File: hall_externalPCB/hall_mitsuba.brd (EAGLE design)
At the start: 100 x 100 mm, 7 parts, among them J1 HEADER_SIDE_5POS, U1 HALLSOT23W, U2 HALLSOT23W, U3 HALLSOT23W

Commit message: placed 8-pin connector
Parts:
- added U$1: HEADER8DEFAULT, Custom_new:8PINVALULOK
- moved J1 35.2 mm to (9.94, 30.5)
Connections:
- removed net N$2: J1.1, U1.2
- removed net N$4: J1.3, U3.2
- removed net N$7: J1.2, U2.2
- new net HALL_A: J1.1, U$1.4, U1.2
- new net HALL_B: J1.2, U$1.3, U2.2
- new net HALL_C: J1.3, U$1.5, U3.2
- net +5V: now also U$1.2
- net GND: now also U$1.1
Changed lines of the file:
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@@
 <drawing>
 <settings>
-<setting alwaysvectorfont="yes"/>
+<setting alwaysvectorfont="no"/>
 <setting verticaltext="up"/>
 </settings>
@@
 <element name="C2" library="rcl" package="C0603" value="0.1uF" x="-31.568" y="31.57" rot="MR315"/>
 <element name="C3" library="rcl" package="C0603" value="0.1uF" x="-27.217996875" y="35.57" rot="MR322.5"/>
-<element name="J1" library="sc_usercreated" package="HEADER_SIDE_5POS" value="HEADER_SIDE_5POS" x="-24.06" y="21.48"/>
+<element name="J1" library="sc_usercreated" package="HEADER_SIDE_5POS" value="HEADER_SIDE_5POS" x="9.94" y="30.48"/>
 <element name="U1" library="Custom_new" package="SOT23W" value="HALLSOT23W" x="-38.080959375" y="29.22055" rot="MR307.5"/>
 <element name="U2" library="Custom_new" package="SOT23W" value="HALLSOT23W" x="-33.941125" y="33.941125" rot="MR315"/>
 <element name="U3" library="Custom_new" package="SOT23W" value="HALLSOT23W" x="-29.22055" y="38.080959375" rot="MR322.5"/>
+<element name="U$1" library="Custom_new" package="8PINVALULOK" value="HEADER8DEFAULT" x="-20.099509375" y="11.189965625" rot="R45"/>
 </elements>
 <signals>
@@
 <contactref element="C3" pad="1"/>
 <contactref element="J1" pad="4"/>
-<wire x1="-27.67365" y1="37.62554375" x2="-24.06" y2="18.94" width="0" layer="19" extent="1-1"/>
-<wire x1="-32.348015625" y1="33.691515625" x2="-27.67365" y2="37.62554375" width="0" layer="19" extent="1-1"/>
-<wire x1="-36.468896875" y1="29.18101875" x2="-32.348015625" y2="33.691515625" width="0" layer="19" extent="1-1"/>
-<wire x1="-34.90055" y1="27.85435" x2="-27.67365" y2="37.62554375" width="0" layer="19" extent="1-1"/>
-<wire x1="-30.966959375" y1="32.171040625" x2="-36.468896875" y2="29.18101875" width="0" layer="19" extent="1-1"/>
-<wire x1="-26.543646875" y1="36.087446875" x2="-30.966959375" y2="32.171040625" width="0" layer="19" extent="1-1"/>
+<contactref element="U$1" pad="2"/>
+<wire x1="-20.099509375" y1="11.189965625" x2="9.94" y2="27.94" width="0" layer="19" extent="1-1"/>
+<wire x1="-34.90055" y1="27.85435" x2="-20.099509375" y2="11.189965625" width="0" layer="19" extent="16-16"/>
+<wire x1="-36.468896875" y1="29.18101875" x2="-34.90055" y2="27.85435" width="0" layer="19" extent="16-16"/>
+<wire x1="-30.966959375" y1="32.171040625" x2="-34.90055" y2="27.85435" width="0" layer="19" extent="16-16"/>
+<wire x1="-32.348015625" y1="33.691515625" x2="-30.966959375" y2="32.171040625" width="0" layer="19" extent="16-16"/>
+<wire x1="-26.543646875" y1="36.087446875" x2="-30.966959375" y2="32.171040625" width="0" layer="19" extent="16-16"/>
+<wire x1="-27.67365" y1="37.625540625" x2="-26.543646875" y2="36.087446875" width="0" layer="19" extent="16-16"/>
 </signal>
 <signal name="GND">
@@
 <contactref element="C3" pad="2"/>
 <contactref element="J1" pad="5"/>
-<wire x1="-35.935446875" y1="26.505646875" x2="-24.06" y2="16.4" width="0" layer="19" extent="1-1"/>
-<wire x1="-30.01376875" y1="39.1147" x2="-35.935446875" y2="26.505646875" width="0" layer="19" extent="1-1"/>
-<wire x1="-34.8624875" y1="34.862484375" x2="-30.01376875" y2="39.1147" width="0" layer="19" extent="1-1"/>
-<wire x1="-27.89235" y1="35.05255" x2="-34.8624875" y2="34.862484375" width="0" layer="19" extent="1-1"/>
-<wire x1="-32.16904375" y1="30.96895625" x2="-27.89235" y2="35.05255" width="0" layer="19" extent="1-1"/>
-<wire x1="-39.1147" y1="30.013765625" x2="-32.16904375" y2="30.96895625" width="0" layer="19" extent="1-1"/>
+<contactref element="U$1" pad="1"/>
+<wire x1="-23.98859375" y1="15.07905" x2="9.94" y2="25.4" width="0" layer="19" extent="1-1"/>
+<wire x1="-35.935446875" y1="26.505646875" x2="-23.98859375" y2="15.07905" width="0" layer="19" extent="16-16"/>
+<wire x1="-39.1147" y1="30.013765625" x2="-35.935446875" y2="26.505646875" width="0" layer="19" extent="16-16"/>
+<wire x1="-32.16904375" y1="30.96895625" x2="-35.935446875" y2="26.505646875" width="0" layer="19" extent="16-16"/>
+<wire x1="-34.8624875" y1="34.862484375" x2="-32.16904375" y2="30.96895625" width="0" layer="19" extent="16-16"/>
+<wire x1="-27.89235" y1="35.05255" x2="-32.16904375" y2="30.96895625" width="0" layer="19" extent="16-16"/>
+<wire x1="-30.01376875" y1="39.114696875" x2="-27.89235" y2="35.05255" width="0" layer="19" extent="16-16"/>
 </signal>
-<signal name="N$2">
+<signal name="HALL_B">
+<contactref element="U$1" pad="3"/>
+<contactref element="U2" pad="2"/>
+<contactref element="J1" pad="2"/>
+<wire x1="-21.018746875" y1="18.0489" x2="9.94" y2="33.02" width="0" layer="19" extent="1-1"/>
+<wire x1="-33.69151875" y1="32.3480125" x2="-21.018746875" y2="18.0489" width="0" layer="19" extent="16-16"/>
+</signal>
+<signal name="HALL_A">
+<contactref element="U$1" pad="4"/>
 <contactref element="U1" pad="2"/>
 <contactref element="J1" pad="1"/>
-<wire x1="-37.62554375" y1="27.673646875" x2="-24.06" y2="26.56" width="0" layer="19" extent="1-1"/>
+<wire x1="-17.129659375" y1="14.1598125" x2="9.94" y2="35.56" width="0" layer="19" extent="1-1"/>
+<wire x1="-37.62554375" y1="27.673646875" x2="-17.129659375" y2="14.1598125" width="0" layer="19" extent="16-16"/>
 </signal>
-<signal name="N$4">
+<signal name="HALL_C">
+<contactref element="U$1" pad="5"/>
 <contactref element="U3" pad="2"/>
 <contactref element="J1" pad="3"/>
-<wire x1="-29.181021875" y1="36.468896875" x2="-24.06" y2="21.48" width="0" layer="19" extent="1-1"/>
-</signal>
-<signal name="N$7">
-<contactref element="U2" pad="2"/>
-<contactref element="J1" pad="2"/>
-<wire x1="-33.69151875" y1="32.3480125" x2="-24.06" y2="24.02" width="0" layer="19" extent="1-1"/>
+<wire x1="-18.048896875" y1="21.018746875" x2="9.94" y2="30.48" width="0" layer="19" extent="1-1"/>
+<wire x1="-29.181021875" y1="36.46889375" x2="-18.048896875" y2="21.018746875" width="0" layer="19" extent="16-16"/>
 </signal>
 </signals>

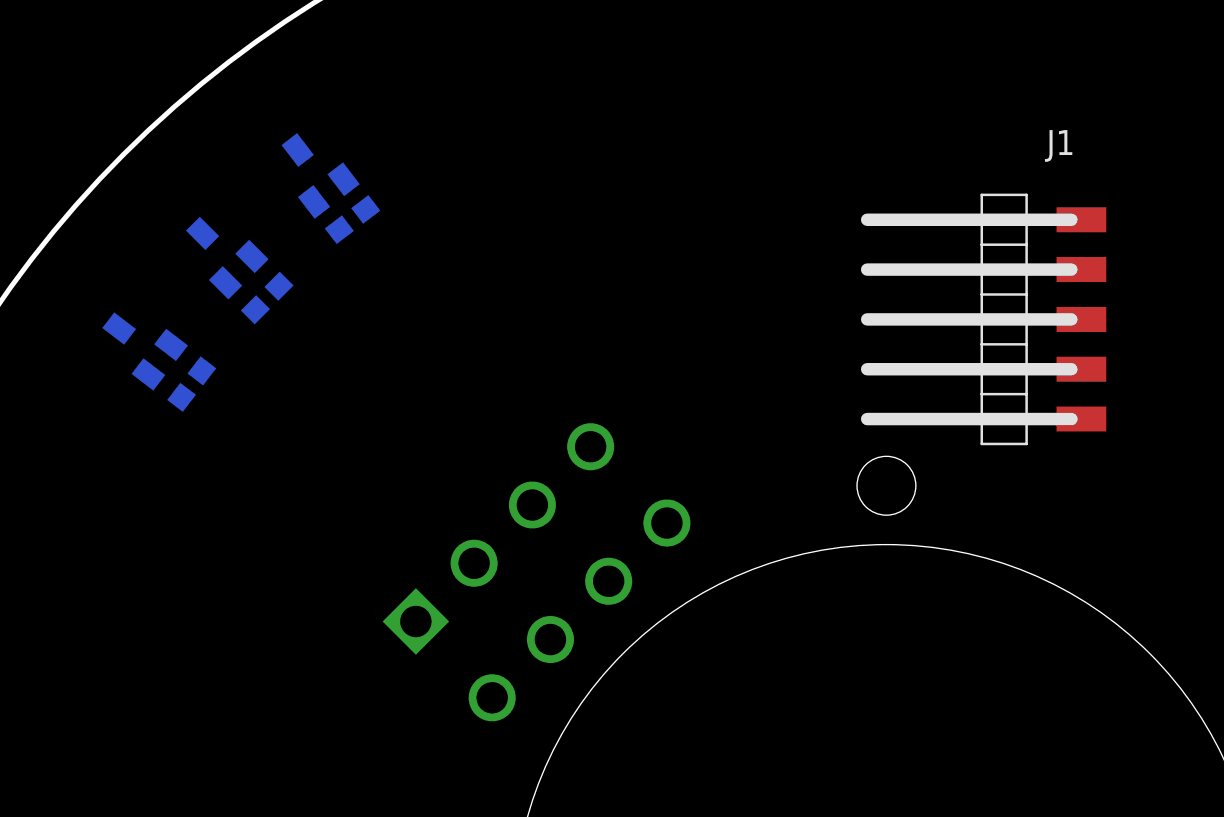
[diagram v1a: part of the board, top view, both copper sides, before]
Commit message: routed halls - TODO: sensorless voltage dividers
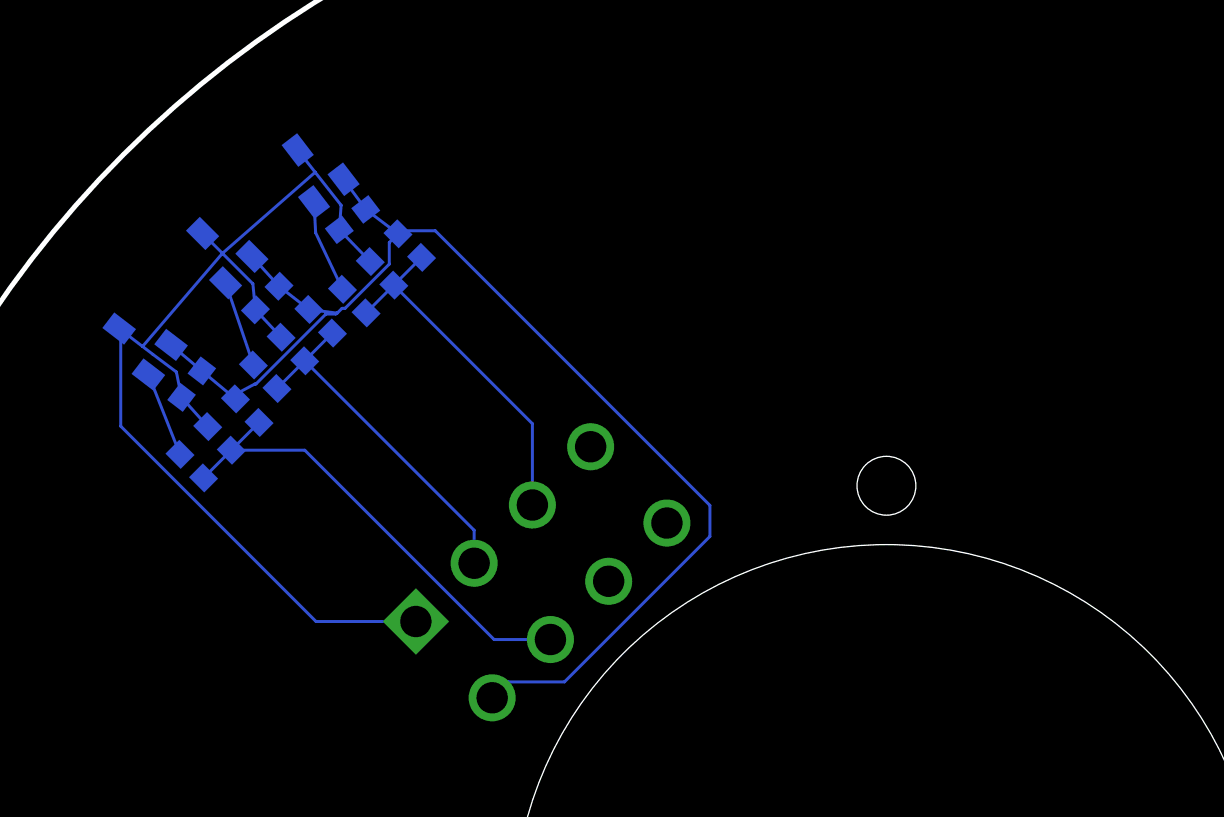
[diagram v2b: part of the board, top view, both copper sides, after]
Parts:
- removed J1: HEADER_SIDE_5POS, sc_usercreated:HEADER_SIDE_5POS
- added C4, C5, C6: (no value), SparkFun-Passives:0603-CAP
- added R1, R2, R3, R4, R5, R6: (no value), SparkFun-Passives:0603-RES
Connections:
- new net HALL_A_RAW: R4.2, U1.2
- new net HALL_B_RAW: R5.2, U2.2
- new net HALL_C_RAW: R6.2, U3.2
- net +5V: now also R1.2, R2.2, R3.2; no longer J1.4
- net GND: now also C4.2, C5.2, C6.2; no longer J1.5
- net HALL_A: now also C4.1, R1.1, R4.1; no longer J1.1, U1.2
- net HALL_B: now also C5.1, R2.1, R5.1; no longer J1.2, U2.2
- net HALL_C: now also C6.1, R3.1, R6.1; no longer J1.3, U3.2
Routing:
- net +5V: track 0.00 -> 63.9 mm
- net GND: track 0.00 -> 57.6 mm
- net HALL_A: track 0.00 -> 24.3 mm
- net HALL_C: track 0.00 -> 18.1 mm
- net HALL_B: track 0.00 -> 17.9 mm
- net HALL_C_RAW: track 0.00 -> 4.76 mm
- net HALL_B_RAW: track 0.00 -> 4.42 mm
- net HALL_A_RAW: track 0.00 -> 4.38 mm

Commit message: mitsuba hall CAM first pass test
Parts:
- added U$2, U$3: (no value), Custom_old:DEV
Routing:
- added copper zone on layer 1, net GND
- added copper zone on layer 16, net GND
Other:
- board text added: "3x hall sensors 7.5° separation centered 45° from vertical"
- board text added: "Mitsuba Hall Sensor PCB mount test Designed Feb 22, 2019 by Gerry Chen"
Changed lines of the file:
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@@
 <drawing>
 <settings>
-<setting alwaysvectorfont="no"/>
+<setting alwaysvectorfont="yes"/>
 <setting verticaltext="up"/>
 </settings>
@@
 <layer number="27" name="tValues" color="7" fill="1" visible="yes" active="yes"/>
 <layer number="28" name="bValues" color="7" fill="1" visible="yes" active="yes"/>
-<layer number="29" name="tStop" color="7" fill="3" visible="no" active="yes"/>
-<layer number="30" name="bStop" color="7" fill="6" visible="no" active="yes"/>
+<layer number="29" name="tStop" color="7" fill="3" visible="yes" active="yes"/>
+<layer number="30" name="bStop" color="7" fill="6" visible="yes" active="yes"/>
 <layer number="31" name="tCream" color="7" fill="4" visible="no" active="yes"/>
 <layer number="32" name="bCream" color="7" fill="5" visible="no" active="yes"/>
@@
 <wire x1="22.9129" y1="50" x2="-22.9129" y2="50" width="0.254" layer="20"/>
 <text x="-67" y="48" size="1.778" layer="49">240° / (32 poles) = 7.5° separation</text>
+<text x="1" y="42" size="1.27" layer="21" font="vector" ratio="15" align="center">Mitsuba Hall Sensor PCB mount test
+Designed Feb 22, 2019 by Gerry Chen</text>
+<text x="0" y="33" size="1.27" layer="21" font="vector" ratio="15" align="center">3x hall sensors
+7.5° separation
+centered 45° from vertical</text>
 </plain>
 <attributes>
@@
 <element name="C5" library="SparkFun-Passives" package="0603-CAP" value="" x="-30.25735625" y="28.971571875" rot="MR45"/>
 <element name="C6" library="SparkFun-Passives" package="0603-CAP" value="" x="-25.714715625" y="32.82893125" rot="MR45"/>
+<element name="U$2" library="Custom_old" package="DEV" value="" x="-43" y="10"/>
+<element name="U$3" library="Custom_old" package="DEV" value="" x="29" y="1"/>
 </elements>
 <signals>
@@
 <wire x1="-39.03578125" y1="25.03578125" x2="-39.03578125" y2="29.9533" width="0.1524" layer="16"/>
 <wire x1="-29.07905" y1="15.07905" x2="-39.03578125" y2="25.03578125" width="0.1524" layer="16"/>
+<polygon width="0.1524" layer="1">
+<vertex x="-49" y="-23"/>
+<vertex x="-49" y="24"/>
+<vertex x="-23" y="50"/>
+<vertex x="23" y="50"/>
+<vertex x="50" y="23"/>
+<vertex x="50" y="-23"/>
+<vertex x="23" y="-50"/>
+<vertex x="-22" y="-50"/>
+</polygon>
+<polygon width="0.1524" layer="1">
+<vertex x="-49" y="-23"/>
+<vertex x="-49" y="24"/>
+<vertex x="-23" y="50"/>
+<vertex x="23" y="50"/>
+<vertex x="50" y="23"/>
+<vertex x="50" y="-23"/>
+<vertex x="23" y="-50"/>
+<vertex x="-22" y="-50"/>
+</polygon>
+<polygon width="0.1524" layer="16">
+<vertex x="-49" y="-25"/>
+<vertex x="-49" y="24"/>
+<vertex x="-23" y="50"/>
+<vertex x="23" y="50"/>
+<vertex x="50" y="23"/>
+<vertex x="50" y="-23"/>
+<vertex x="23" y="-50"/>
+<vertex x="-24" y="-50"/>
+</polygon>
 </signal>
 <signal name="HALL_B">
@@
 </drawing>
 <compatibility>
+<note version="6.3" minversion="6.2.2" severity="warning">
+Since Version 6.2.2 text objects can contain more than one line,
+which will not be processed correctly with this version.
+</note>
 <note version="8.3" severity="warning">
 Since Version 8.3, EAGLE supports Fusion synchronisation.

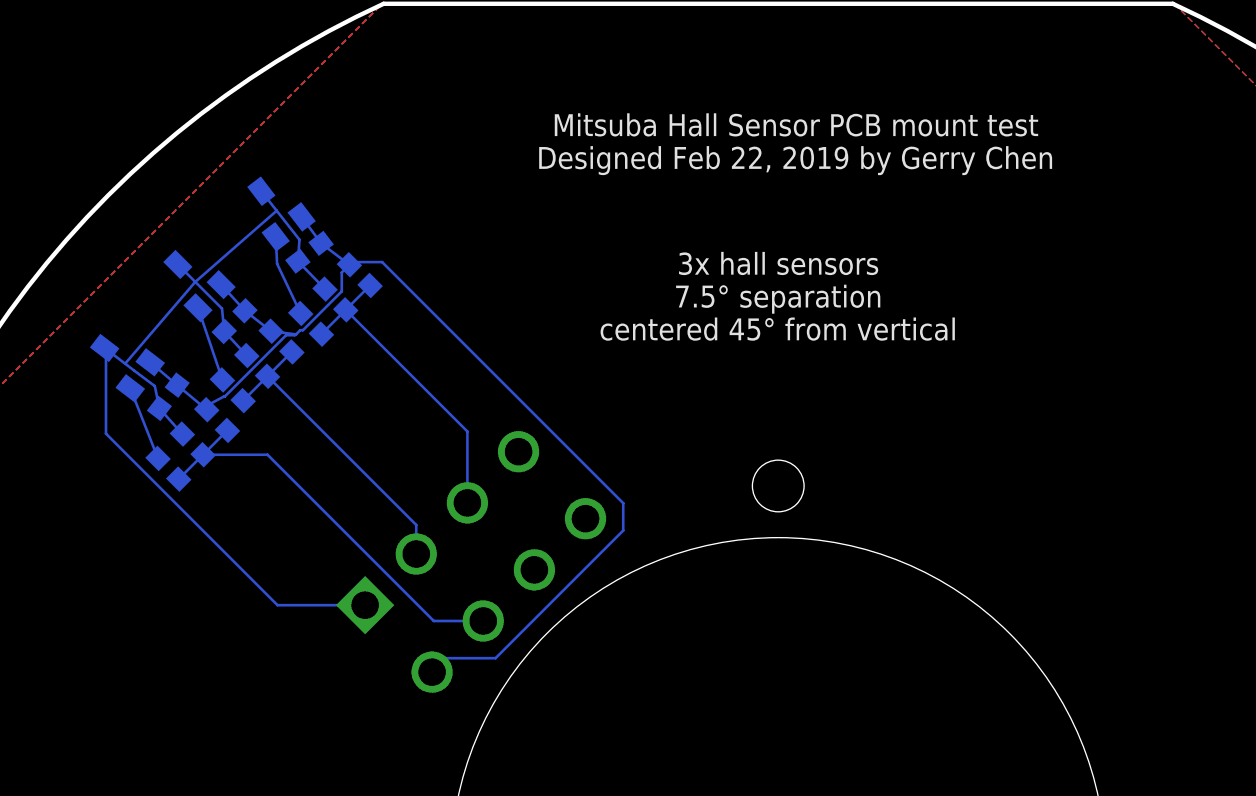
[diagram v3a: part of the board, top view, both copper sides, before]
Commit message: modified external hall mitsuba and also started on internal mitsuba controller
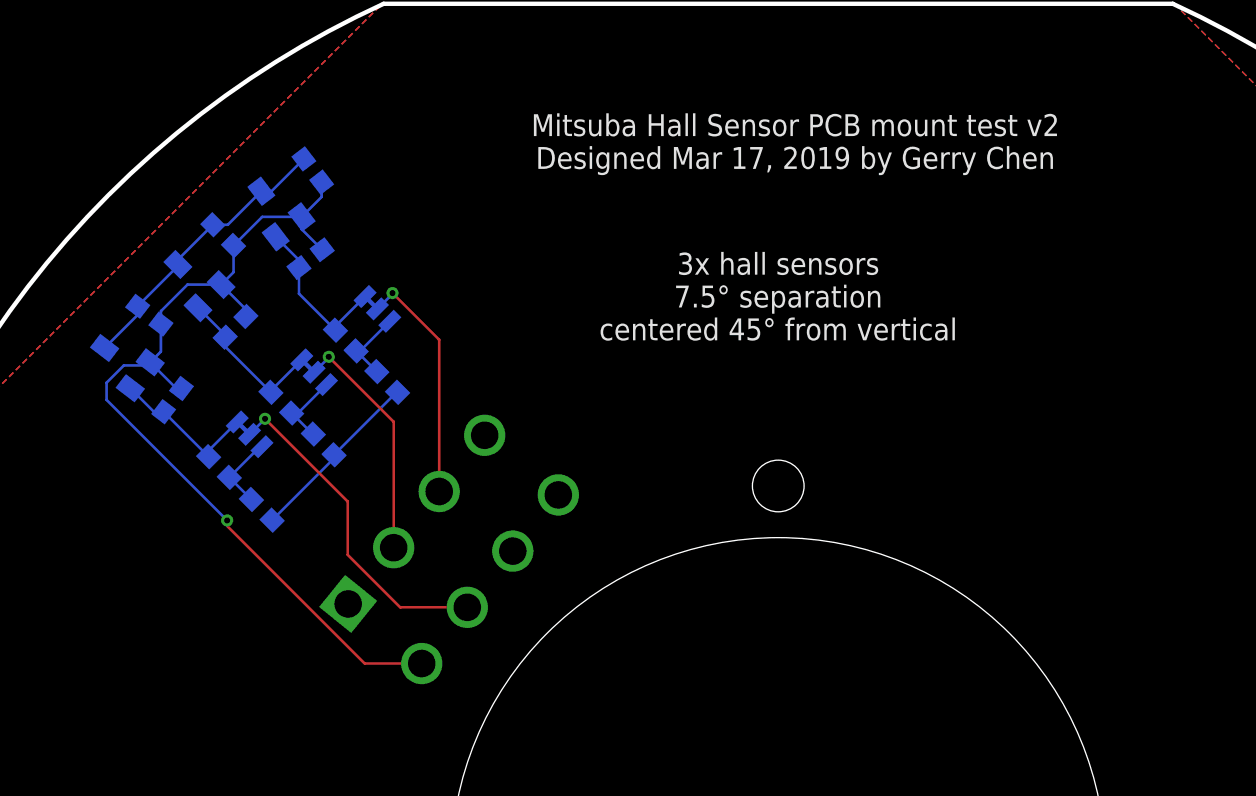
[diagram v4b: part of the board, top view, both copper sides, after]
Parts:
- added JP1, JP2, JP3: (no value), SparkFun-Jumpers:SMT-JUMPER_3_1-NC_TRACE_SILK
- C1, C2, C3: device rcl:C0603 -> SparkFun-Passives:0603-CAP
- C4, C5, C6: value (none) -> 4.7n
- R1, R2, R3: value (none) -> 2.2k
- R4, R5, R6: value (none) -> 10k
- U1, U2, U3: value HALLSOT23W -> HALL_SOT23W
- moved C5 5.97 mm to (-26.4, 24.4), turned to 225 degrees
- moved C6 5.65 mm to (-22.7, 28.0), turned to 225 degrees
- moved C4 5.52 mm to (-30.0, 20.6), turned to 225 degrees
- moved C2 5.04 mm to (-32.2, 36.6), turned to 45 degrees
- moved C1 4.86 mm to (-36.5, 31.9), turned to 37.5 degrees
- moved C3 4.75 mm to (-27.0, 40.3), turned to 52.5 degrees
- moved R3 3.01 mm to (-27.2, 35.2), turned to 142.5 degrees
- moved R4 2.94 mm to (-32.5, 23.1)
- moved R5 2.90 mm to (-28.9, 26.8)
- moved R1 2.83 mm to (-35.2, 27.0), turned to 127.5 degrees
- moved R2 2.81 mm to (-31.5, 31.2), turned to 135 degrees
- moved R6 2.24 mm to (-25.1, 30.4)
- moved U$1 0.78 mm to (-20.7, 11.7), turned to 51 degrees
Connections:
- new net HALL_A_OUT: JP2.2, U$1.4
- new net HALL_B_OUT: JP3.2, U$1.3
- new net HALL_C_OUT: JP1.2, U$1.5
- net HALL_A: now also JP2.1; no longer R1.1, U$1.4
- net HALL_A_RAW: now also JP2.3, R1.1
- net HALL_B: now also JP3.1; no longer R2.1, U$1.3
- net HALL_B_RAW: now also JP3.3, R2.1
- net HALL_C: now also JP1.1; no longer R3.1, U$1.5
- net HALL_C_RAW: now also JP1.3, R3.1
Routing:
- net GND: track 57.6 -> 27.1 mm
- net HALL_A: track 24.3 -> 4.45 mm
- net HALL_A_OUT: track 0.00 -> 19.4 mm, vias 0 -> 1
- net HALL_C_OUT: track 0.00 -> 13.9 mm, vias 0 -> 1
- net HALL_B_OUT: track 0.00 -> 13.9 mm, vias 0 -> 1
- net HALL_C: track 18.1 -> 4.37 mm
- net HALL_B: track 17.9 -> 4.48 mm
- net +5V: track 63.9 -> 53.2 mm, vias 0 -> 1
- net HALL_B_RAW: track 4.42 -> 9.29 mm
- net HALL_C_RAW: track 4.76 -> 9.53 mm
- net HALL_A_RAW: track 4.38 -> 8.90 mm
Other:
- board text added: "Mitsuba Hall Sensor PCB mount test v2 Designed Mar 17, 2019 by Gerry Chen"
- board text removed: "Mitsuba Hall Sensor PCB mount test Designed Feb 22, 2019 by Gerry Chen"
